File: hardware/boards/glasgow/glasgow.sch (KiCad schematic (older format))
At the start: 90 parts, among them J1 USB_B_Micro, U1 CY7C68013A-56LTX, U15 TPD3S014, U2 CAT24M01W, U3 CAT24C256W, U30 ICE40HX8K-BG121, U34 ATECC508A, U7 LM3880MF-1AF, U8 MIC5355-S4YMME, Y1 24M

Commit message: revC1: clean up some datasheet links & MPNs
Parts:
- R15: MPN RC0402FR-132k2L -> RC0402FR-132K2L
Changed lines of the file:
@@
 F 1 "18p" V 2350 2450 50  0000 C CNN
 F 2 "Capacitor_SMD:C_0402_1005Metric" H 2238 2300 50  0001 C CNN
-F 3 "https://www.mouser.hk/datasheet/2/447/UPY-GP_NP0_16V-to-50V_16-1109089.pdf" H 2200 2450 50  0001 C CNN
+F 3 "https://www.mouser.com/datasheet/2/447/UPY-GP_NP0_16V-to-50V_16-1109089.pdf" H 2200 2450 50  0001 C CNN
 F 4 "Yageo" H 650 -250 50  0001 C CNN "Mfg"
 F 5 "CC0402JRNPO8BN180" H 650 -250 50  0001 C CNN "MPN"
@@
 F 1 "1M" V 1100 5450 50  0000 C CNN
 F 2 "Resistor_SMD:R_0402_1005Metric" V 1030 5450 50  0001 C CNN
-F 3 "https://www.mouser.com/datasheet/2/447/PYu-RC_Group_51_RoHS_L_9-1314892.pdf" H 1100 5450 50  0001 C CNN
+F 3 "https://www.mouser.com/datasheet/2/447/PYu-RC_Group_51_RoHS_L_10-1527934.pdf" H 1100 5450 50  0001 C CNN
 F 4 "Yageo" H -50 400 50  0001 C CNN "Mfg"
 F 5 "RC0402FR-131ML" H -50 400 50  0001 C CNN "MPN"
@@
 F 1 "18p" V 2350 2950 50  0000 C CNN
 F 2 "Capacitor_SMD:C_0402_1005Metric" H 2238 2800 50  0001 C CNN
-F 3 "https://www.mouser.hk/datasheet/2/447/UPY-GP_NP0_16V-to-50V_16-1109089.pdf" H 2200 2950 50  0001 C CNN
+F 3 "https://www.mouser.com/datasheet/2/447/UPY-GP_NP0_16V-to-50V_16-1109089.pdf" H 2200 2950 50  0001 C CNN
 F 4 "Yageo" H 650 -250 50  0001 C CNN "Mfg"
 F 5 "CC0402JRNPO8BN180" H 650 -250 50  0001 C CNN "MPN"
@@
 F 1 "2k2" V 2650 4700 50  0000 C CNN
 F 2 "Resistor_SMD:R_0402_1005Metric" V 2580 4700 50  0001 C CNN
-F 3 "https://www.mouser.com/datasheet/2/447/PYu-RC_Group_51_RoHS_L_9-1314892.pdf" H 2650 4700 50  0001 C CNN
+F 3 "https://www.mouser.com/datasheet/2/447/PYu-RC_Group_51_RoHS_L_10-1527934.pdf" H 2650 4700 50  0001 C CNN
 F 4 "Yageo" H 650 -250 50  0001 C CNN "Mfg"
 F 5 "RC0402FR-132K2L" H 650 -250 50  0001 C CNN "MPN"
@@
 F 1 "100k" V 8500 5850 50  0000 R CNN
 F 2 "Resistor_SMD:R_0402_1005Metric" V 8430 5750 50  0001 C CNN
-F 3 "https://www.mouser.com/datasheet/2/447/PYu-RC_Group_51_RoHS_L_9-1314892.pdf" H 8500 5750 50  0001 C CNN
+F 3 "https://www.mouser.com/datasheet/2/447/PYu-RC_Group_51_RoHS_L_10-1527934.pdf" H 8500 5750 50  0001 C CNN
 F 4 "Yageo" H -450 0   50  0001 C CNN "Mfg"
 F 5 "RC0402FR-13100KL" H -450 0   50  0001 C CNN "MPN"
@@
 F 1 "100k" V 8500 5950 50  0000 R CNN
 F 2 "Resistor_SMD:R_0402_1005Metric" V 8430 5850 50  0001 C CNN
-F 3 "https://www.mouser.com/datasheet/2/447/PYu-RC_Group_51_RoHS_L_9-1314892.pdf" H 8500 5850 50  0001 C CNN
+F 3 "https://www.mouser.com/datasheet/2/447/PYu-RC_Group_51_RoHS_L_10-1527934.pdf" H 8500 5850 50  0001 C CNN
 F 4 "Yageo" H -450 0   50  0001 C CNN "Mfg"
 F 5 "RC0402FR-13100KL" H -450 0   50  0001 C CNN "MPN"
@@
 F 1 "100k" V 2800 3350 50  0000 C CNN
 F 2 "Resistor_SMD:R_0402_1005Metric" V 2730 3350 50  0001 C CNN
-F 3 "https://www.mouser.com/datasheet/2/447/PYu-RC_Group_51_RoHS_L_9-1314892.pdf" H 2800 3350 50  0001 C CNN
+F 3 "https://www.mouser.com/datasheet/2/447/PYu-RC_Group_51_RoHS_L_10-1527934.pdf" H 2800 3350 50  0001 C CNN
 F 4 "Yageo" H 650 -250 50  0001 C CNN "Mfg"
 F 5 "RC0402FR-13100KL" H 650 -250 50  0001 C CNN "MPN"
@@
 F 1 "100k" V 8750 4600 50  0000 C CNN
 F 2 "Resistor_SMD:R_0402_1005Metric" V 8680 4600 50  0001 C CNN
-F 3 "https://www.mouser.com/datasheet/2/447/PYu-RC_Group_51_RoHS_L_9-1314892.pdf" H 8750 4600 50  0001 C CNN
+F 3 "https://www.mouser.com/datasheet/2/447/PYu-RC_Group_51_RoHS_L_10-1527934.pdf" H 8750 4600 50  0001 C CNN
 F 4 "Yageo" H 1750 -1350 50  0001 C CNN "Mfg"
 F 5 "RC0402FR-13100KL" H 1750 -1350 50  0001 C CNN "MPN"
@@
 F 1 "220k" V 8750 4200 50  0000 C CNN
 F 2 "Resistor_SMD:R_0402_1005Metric" V 8680 4200 50  0001 C CNN
-F 3 "https://www.mouser.hk/datasheet/2/447/PYu-RC_Group_51_RoHS_L_9-1314892.pdf" H 8750 4200 50  0001 C CNN
+F 3 "https://www.mouser.com/datasheet/2/447/PYu-RC_Group_51_RoHS_L_10-1527934.pdf" H 8750 4200 50  0001 C CNN
 F 4 "Yageo" H 1750 -1350 50  0001 C CNN "Mfg"
 F 5 "RC0402FR-13220KL" H 1750 -1350 50  0001 C CNN "MPN"
@@
 F 1 "100k" V 7600 1750 50  0000 C CNN
 F 2 "Resistor_SMD:R_0402_1005Metric" V 7530 1750 50  0001 C CNN
-F 3 "https://www.mouser.com/datasheet/2/447/PYu-RC_Group_51_RoHS_L_9-1314892.pdf" H 7600 1750 50  0001 C CNN
+F 3 "https://www.mouser.com/datasheet/2/447/PYu-RC_Group_51_RoHS_L_10-1527934.pdf" H 7600 1750 50  0001 C CNN
 F 4 "Yageo" H 3200 -1800 50  0001 C CNN "Mfg"
 F 5 "RC0402FR-13100KL" H 3200 -1800 50  0001 C CNN "MPN"
@@
 F 1 "20k" V 9450 900 50  0000 C CNN
 F 2 "Resistor_SMD:R_0402_1005Metric" V 9380 900 50  0001 C CNN
-F 3 "https://www.mouser.com/datasheet/2/447/PYu-RC_Group_51_RoHS_L_9-1314892.pdf" H 9450 900 50  0001 C CNN
+F 3 "https://www.mouser.com/datasheet/2/447/PYu-RC_Group_51_RoHS_L_10-1527934.pdf" H 9450 900 50  0001 C CNN
 F 4 "Yageo" H -450 0   50  0001 C CNN "Mfg"
 F 5 "RC0402FR-1320KL" H -450 0   50  0001 C CNN "MPN"
@@
 F 1 "2k2" V 9450 1500 50  0000 C CNN
 F 2 "Resistor_SMD:R_0402_1005Metric" V 9380 1500 50  0001 C CNN
-F 3 "https://www.mouser.com/datasheet/2/447/PYu-RC_Group_51_RoHS_L_9-1314892.pdf" H 9450 1500 50  0001 C CNN
+F 3 "https://www.mouser.com/datasheet/2/447/PYu-RC_Group_51_RoHS_L_10-1527934.pdf" H 9450 1500 50  0001 C CNN
 F 4 "Yageo" H -450 0   50  0001 C CNN "Mfg"
-F 5 "RC0402FR-132k2L" H -450 0   50  0001 C CNN "MPN"
+F 5 "RC0402FR-132K2L" H -450 0   50  0001 C CNN "MPN"
 F 6 "res-0402-2k2" H 9450 1500 50  0001 C CNN "1b2-bom-key"
 	1    9450 1500
@@
 F 1 "10k" V 9450 1700 50  0000 C CNN
 F 2 "Resistor_SMD:R_0402_1005Metric" V 9380 1700 50  0001 C CNN
-F 3 "https://www.mouser.hk/datasheet/2/447/PYu-RC_Group_51_RoHS_L_9-1314892.pdf" H 9450 1700 50  0001 C CNN
+F 3 "https://www.mouser.com/datasheet/2/447/PYu-RC_Group_51_RoHS_L_10-1527934.pdf" H 9450 1700 50  0001 C CNN
 F 4 "Yageo" H -450 0   50  0001 C CNN "Mfg"
 F 5 "RC0402FR-1310KL" H -450 0   50  0001 C CNN "MPN"
@@
 F 1 "20k" V 9450 1100 50  0000 C CNN
 F 2 "Resistor_SMD:R_0402_1005Metric" V 9380 1100 50  0001 C CNN
-F 3 "https://www.mouser.com/datasheet/2/447/PYu-RC_Group_51_RoHS_L_9-1314892.pdf" H 9450 1100 50  0001 C CNN
+F 3 "https://www.mouser.com/datasheet/2/447/PYu-RC_Group_51_RoHS_L_10-1527934.pdf" H 9450 1100 50  0001 C CNN
 F 4 "Yageo" H -450 0   50  0001 C CNN "Mfg"
 F 5 "RC0402FR-1320KL" H -450 0   50  0001 C CNN "MPN"
@@
 F 1 "20k" V 9450 1300 50  0000 C CNN
 F 2 "Resistor_SMD:R_0402_1005Metric" V 9380 1300 50  0001 C CNN
-F 3 "https://www.mouser.com/datasheet/2/447/PYu-RC_Group_51_RoHS_L_9-1314892.pdf" H 9450 1300 50  0001 C CNN
+F 3 "https://www.mouser.com/datasheet/2/447/PYu-RC_Group_51_RoHS_L_10-1527934.pdf" H 9450 1300 50  0001 C CNN
 F 4 "Yageo" H -450 0   50  0001 C CNN "Mfg"
 F 5 "RC0402FR-1320KL" H -450 0   50  0001 C CNN "MPN"
@@
 F 1 "100k" V 5050 4450 50  0000 C CNN
 F 2 "Resistor_SMD:R_0402_1005Metric" V 4980 4450 50  0001 C CNN
-F 3 "https://www.mouser.com/datasheet/2/447/PYu-RC_Group_51_RoHS_L_9-1314892.pdf" H 5050 4450 50  0001 C CNN
+F 3 "https://www.mouser.com/datasheet/2/447/PYu-RC_Group_51_RoHS_L_10-1527934.pdf" H 5050 4450 50  0001 C CNN
 F 4 "Yageo" H 650 -850 50  0001 C CNN "Mfg"
 F 5 "RC0402FR-13100KL" H 650 -850 50  0001 C CNN "MPN"
@@
 F 1 "100k" V 5050 3700 50  0000 R CNN
 F 2 "Resistor_SMD:R_0402_1005Metric" V 4980 3600 50  0001 C CNN
-F 3 "https://www.mouser.com/datasheet/2/447/PYu-RC_Group_51_RoHS_L_9-1314892.pdf" H 5050 3600 50  0001 C CNN
+F 3 "https://www.mouser.com/datasheet/2/447/PYu-RC_Group_51_RoHS_L_10-1527934.pdf" H 5050 3600 50  0001 C CNN
 F 4 "Yageo" H 650 -450 50  0001 C CNN "Mfg"
 F 5 "RC0402FR-13100KL" H 650 -450 50  0001 C CNN "MPN"
@@
 F 1 "100k" V 5050 3200 50  0000 R CNN
 F 2 "Resistor_SMD:R_0402_1005Metric" V 4980 3100 50  0001 C CNN
-F 3 "https://www.mouser.com/datasheet/2/447/PYu-RC_Group_51_RoHS_L_9-1314892.pdf" H 5050 3100 50  0001 C CNN
+F 3 "https://www.mouser.com/datasheet/2/447/PYu-RC_Group_51_RoHS_L_10-1527934.pdf" H 5050 3100 50  0001 C CNN
 F 4 "Yageo" H 650 -100 50  0001 C CNN "Mfg"
 F 5 "RC0402FR-13100KL" H 650 -100 50  0001 C CNN "MPN"
@@
 F 1 "100" V 5500 5100 50  0000 C CNN
 F 2 "Resistor_SMD:R_0402_1005Metric" V 5430 5100 50  0001 C CNN
-F 3 "https://www.mouser.com/datasheet/2/447/PYu-RC_Group_51_RoHS_L_9-1314892.pdf" H 5500 5100 50  0001 C CNN
+F 3 "https://www.mouser.com/datasheet/2/447/PYu-RC_Group_51_RoHS_L_10-1527934.pdf" H 5500 5100 50  0001 C CNN
 F 4 "Yageo" H -2100 3950 50  0001 C CNN "Mfg"
 F 5 "RC0402FR-13100RL" H -2100 3950 50  0001 C CNN "MPN"
@@
 F 1 "100" V 5500 5500 50  0000 C CNN
 F 2 "Resistor_SMD:R_0402_1005Metric" V 5430 5500 50  0001 C CNN
-F 3 "https://www.mouser.com/datasheet/2/447/PYu-RC_Group_51_RoHS_L_9-1314892.pdf" H 5500 5500 50  0001 C CNN
+F 3 "https://www.mouser.com/datasheet/2/447/PYu-RC_Group_51_RoHS_L_10-1527934.pdf" H 5500 5500 50  0001 C CNN
 F 4 "Yageo" H -2100 4350 50  0001 C CNN "Mfg"
 F 5 "RC0402FR-13100RL" H -2100 4350 50  0001 C CNN "MPN"
@@
 F 1 "2k2" V 2550 4700 50  0000 C CNN
 F 2 "Resistor_SMD:R_0402_1005Metric" V 2480 4700 50  0001 C CNN
-F 3 "https://www.mouser.com/datasheet/2/447/PYu-RC_Group_51_RoHS_L_9-1314892.pdf" H 2550 4700 50  0001 C CNN
+F 3 "https://www.mouser.com/datasheet/2/447/PYu-RC_Group_51_RoHS_L_10-1527934.pdf" H 2550 4700 50  0001 C CNN
 F 4 "Yageo" H 650 -250 50  0001 C CNN "Mfg"
 F 5 "RC0402FR-132K2L" H 650 -250 50  0001 C CNN "MPN"

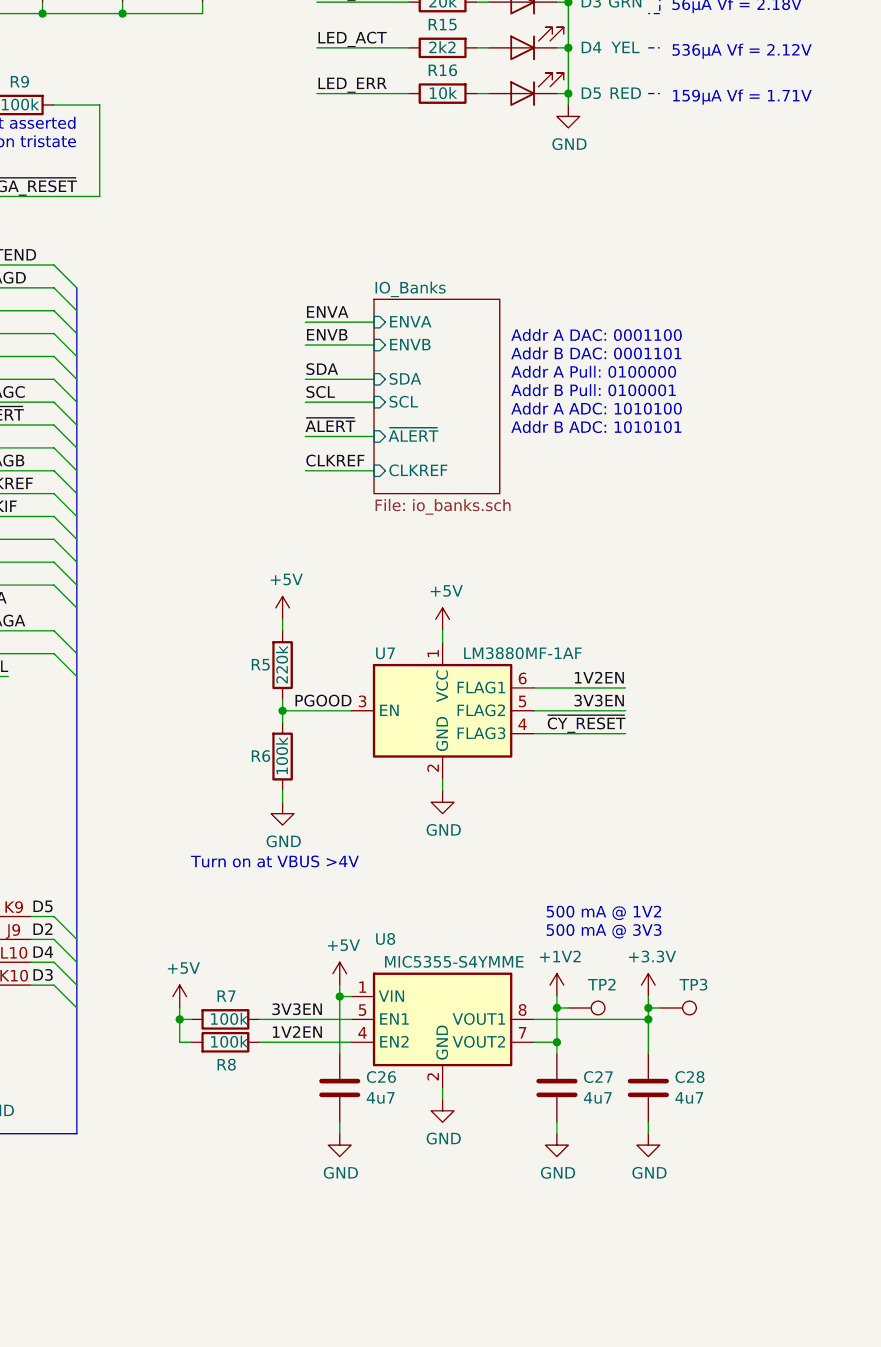
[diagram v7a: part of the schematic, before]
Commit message: revC1: Replace 1V2/3V3 regulator with TLV755/733 series
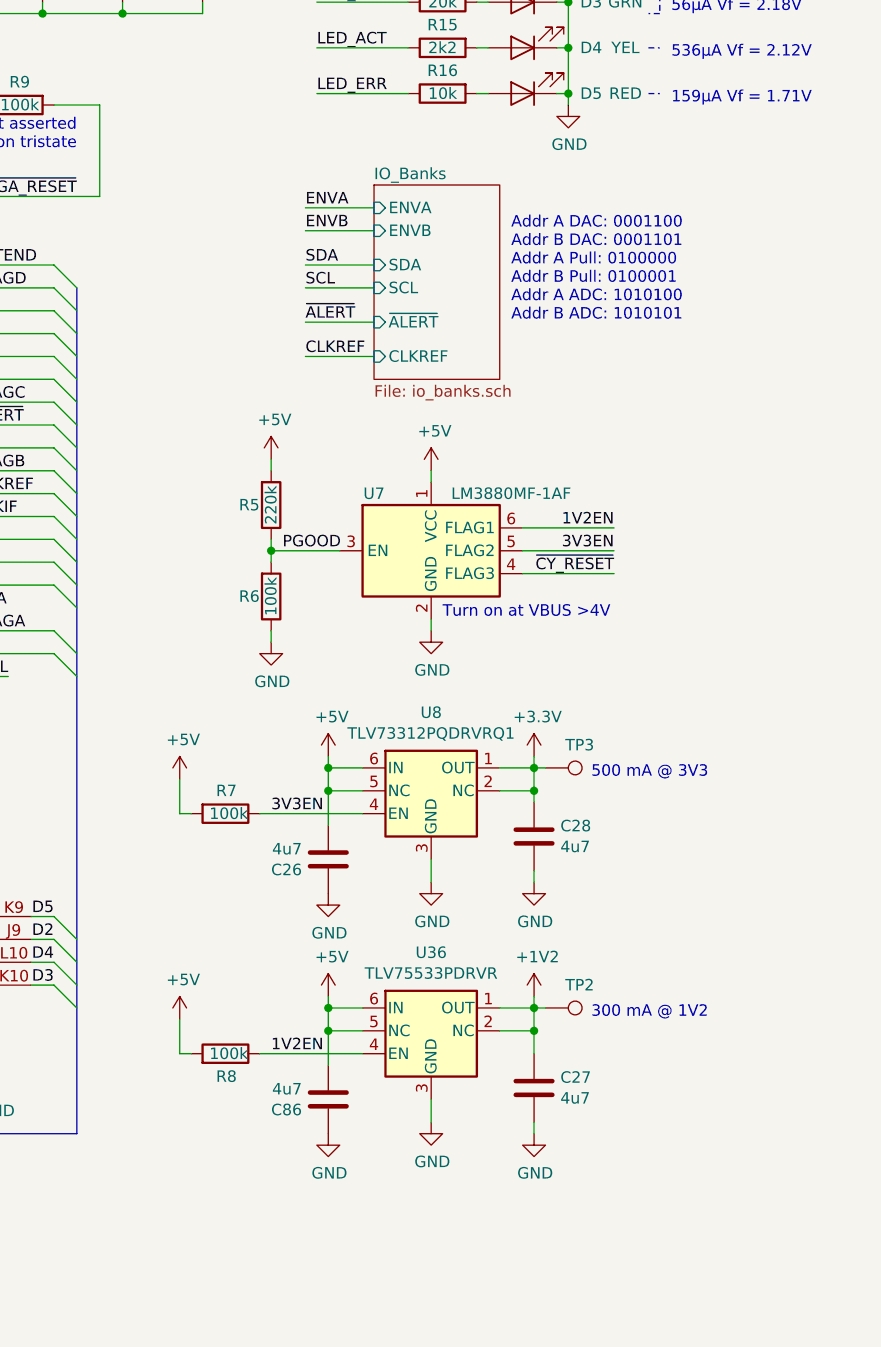
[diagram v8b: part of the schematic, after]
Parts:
- removed U8: MIC5355-S4YMME, Package_SO:MSOP-8-1EP_3x3mm_P0.65mm_EP2.54x2.8mm_ThermalVias, symbol Regulator_Linear:MIC5355-S4YMME
- added C86: 4u7, Capacitor_SMD:C_0603_1608Metric_Pad1.05x0.95mm_HandSolder, symbol Device:C
- added U36: TLV75533PDRVR, Glasgow:DFN-6-1EP_2x2mm_P0.65mm_EP1x1.6mm_ThermalVias, symbol Glasgow:TLV75533PDRVR
- added U8: TLV73312PQDRVRQ1, Glasgow:DFN-6-1EP_2x2mm_P0.65mm_EP1x1.6mm_ThermalVias, symbol Glasgow:TLV73312PQDRVRQ1
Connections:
- net +1V2: now also U36.1 (OUT), U36.2 (NC)
- net +3V3: now also U8.1 (OUT), U8.2 (NC)
- net +5V: now also C26.2, C86.2, U36.5 (NC), U36.6 (IN), U8.5 (NC), U8.6 (IN); no longer C26.1
- net 1V2EN: now also U36.4 (EN)
- net 3V3EN: now also U8.4 (EN)
- net GND: now also C26.1, C86.1, U36.3 (GND), U36.7 (GND), U8.3 (GND), U8.7 (GND); no longer C26.2
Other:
- note added: "300 mA @ 1V2\n"
- note added: "500 mA @ 3V3"
- note removed: "500 mA @ 1V2\n500 mA @ 3V3"
- moved on the sheet: C26, C27, C28, R5, R6, R7, R8, TP2, TP3, U7
